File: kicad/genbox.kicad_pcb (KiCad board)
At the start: 2 copper layers, 336 x 134 mm, 60 parts, among them J1 USB_A, SW15 SW_SPST, SW16 SW_SPST, SW17 SW_SPST, SW18 SW_SPST, U1 DM-OLED096-636, U2 rp2040-zero, U3 SN74LV1T34DBV

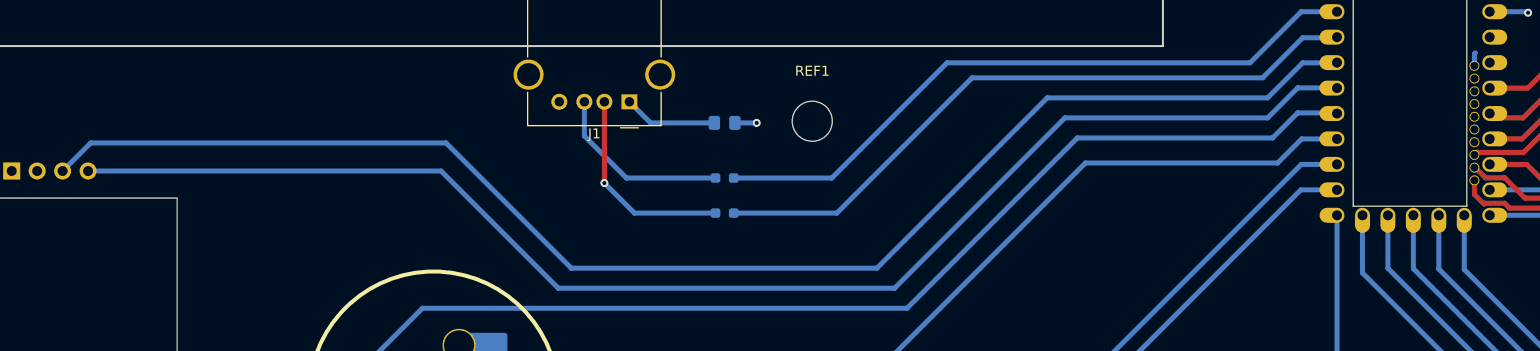
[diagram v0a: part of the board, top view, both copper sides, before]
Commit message: usb a connection switch
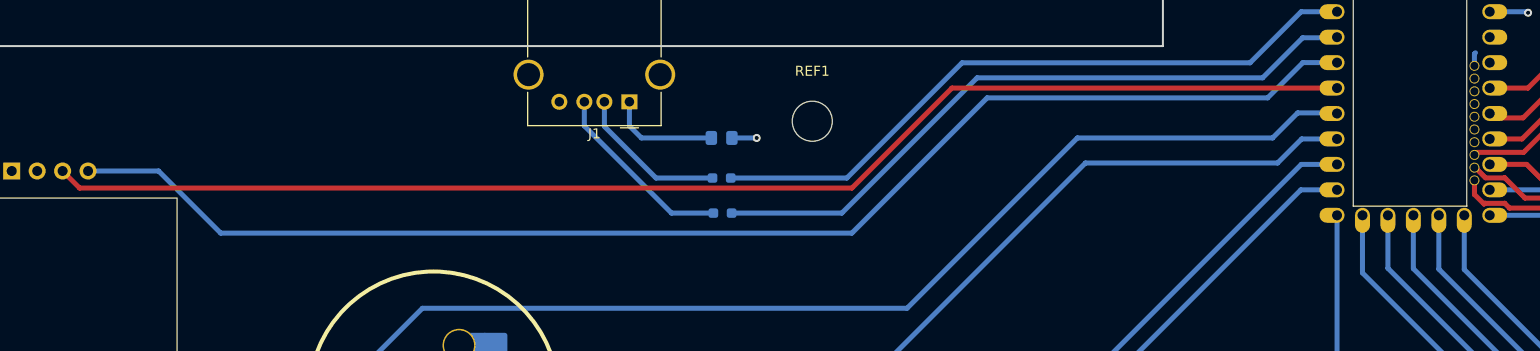
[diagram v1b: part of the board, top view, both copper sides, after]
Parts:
- moved R1 3.51 mm to (143.5, 60.0)
- moved R2 3.51 mm to (143.6, 63.5)
- moved F1 1.53 mm to (143.5, 56.0)
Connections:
- U2 pad 1: USBA D+ -> USBA D-
- U2 pad 2: USBA D- -> USBA D+
- U2 pad 3: OLED SCL -> OLED SDA
- U2 pad 4: OLED SDA -> OLED SCL
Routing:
- net OLED SCL: track 142.0 -> 132.0 mm
- net Net-(J1-D-): track 20.4 -> 15.4 mm, vias 1 -> 0
- net OLED SDA: track 137.8 -> 134.3 mm
- net Net-(J1-VBUS): track 9.35 -> 11.1 mm
- net Net-(J1-D+): track 18.2 -> 18.9 mm
